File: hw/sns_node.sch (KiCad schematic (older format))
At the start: 1 part

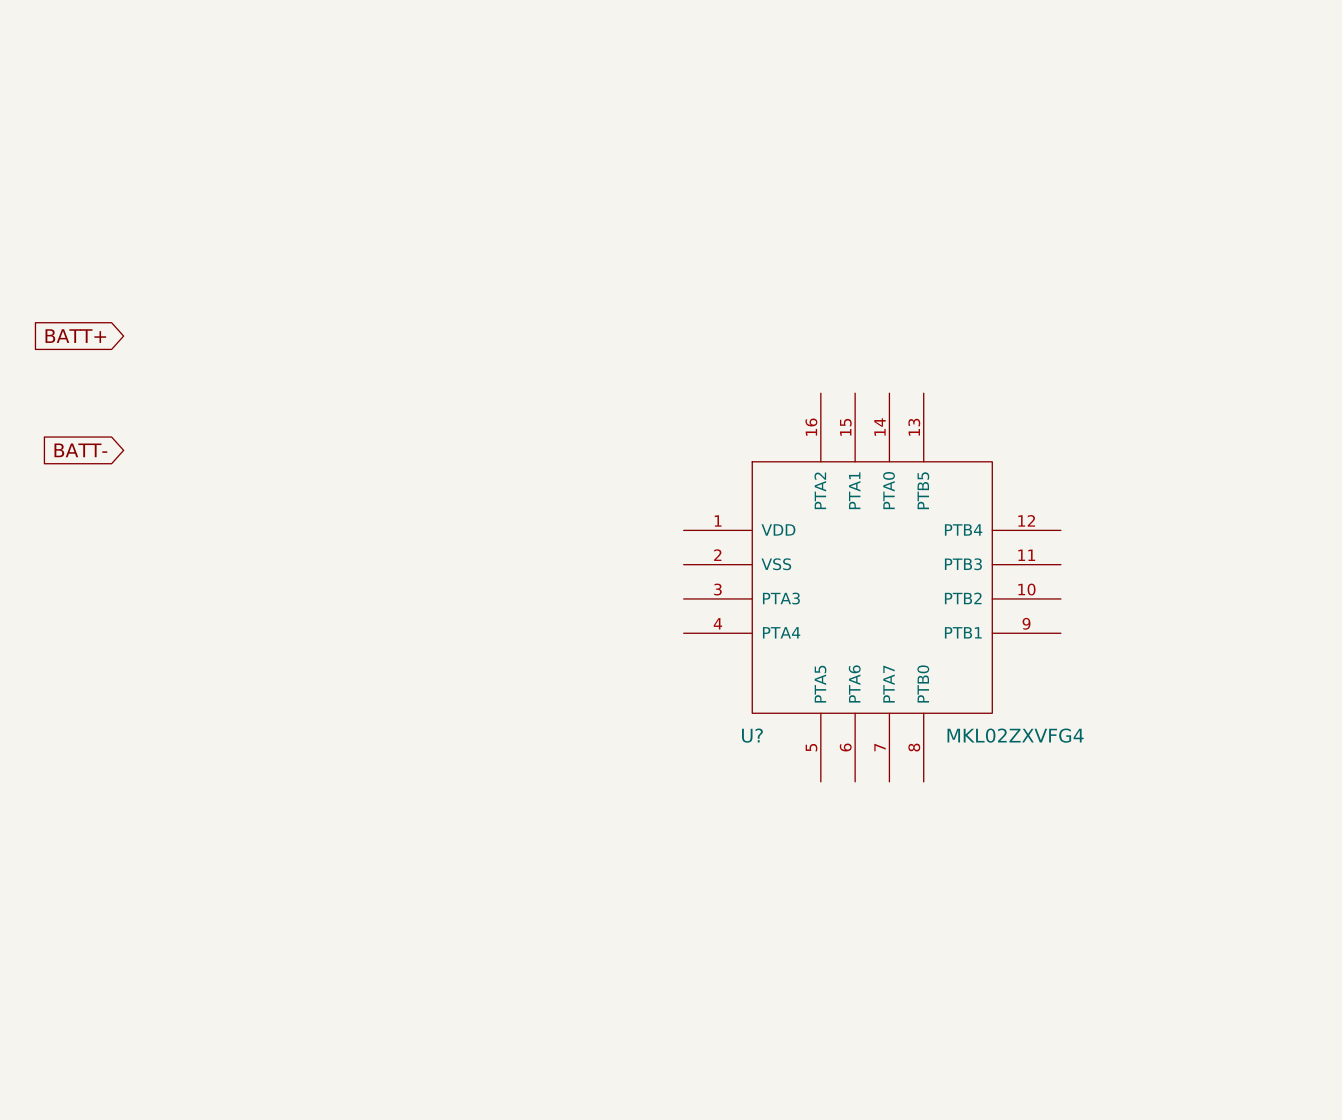
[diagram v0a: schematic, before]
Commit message: - add power supply
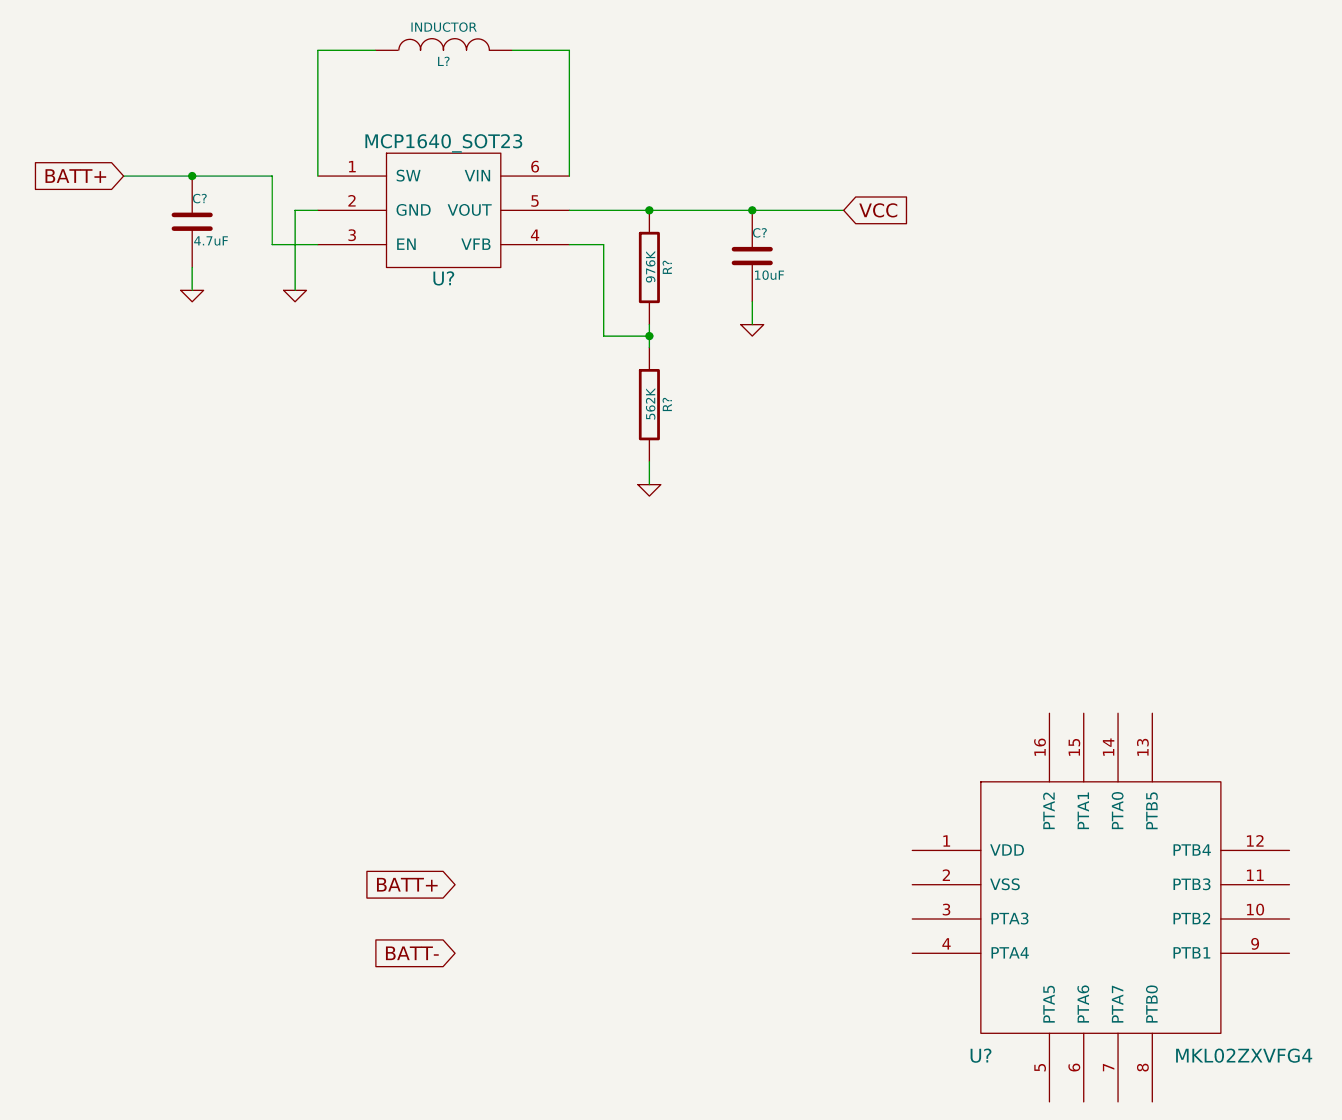
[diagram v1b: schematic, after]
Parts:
- added C?: 4.7uF, ~, symbol C
- added C?: 10uF, ~, symbol C
- added L?: INDUCTOR, ~, symbol INDUCTOR
- added R?: 976K, ~, symbol R
- added R?: 562K, ~, symbol R
- added U?: MCP1640_SOT23, ~, symbol MCP1640_SOT23
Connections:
- net BATT+: now also C?.1, U?.3 (EN)
- new net: L?.1, U?.1 (SW)
- new net: R?.1, R?.2, U?.4 (VFB)
- new net: L?.2, U?.6 (VIN)
- new net GND: C?.2, C?.2, R?.2, U?.2 (GND)
- new net VCC: C?.1, R?.1, U?.5 (VOUT)
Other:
- moved on the sheet: U?
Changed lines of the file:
@@
 L MKL02ZXVFG4 U?
 U 1 1 5302BE68
-P 5400 3350
-F 0 "U?" H 4950 2750 60  0000 C CNN
-F 1 "MKL02ZXVFG4" H 6100 2750 60  0000 C CNN
-F 2 "" H 5400 3350 60  0000 C CNN
-F 3 "" H 5400 3350 60  0000 C CNN
-	1    5400 3350
+P 6400 4750
+F 0 "U?" H 5950 4150 60  0000 C CNN
+F 1 "MKL02ZXVFG4" H 7100 4150 60  0000 C CNN
+F 2 "" H 6400 4750 60  0000 C CNN
+F 3 "" H 6400 4750 60  0000 C CNN
+	1    6400 4750
 	1    0    0    -1
 $EndComp
-Text GLabel 2200 2200 0    60   Input ~ 0
+Text GLabel 2200 1500 0    60   Input ~ 0
 BATT+
-Text GLabel 2200 2700 0    60   Input ~ 0
+Text GLabel 3650 4900 0    60   Input ~ 0
 BATT-
+$Comp
+L MCP1640_SOT23 U?
+U 1 1 5302BFBE
+P 3600 1650
+F 0 "U?" H 3600 1350 60  0000 C CNN
+F 1 "MCP1640_SOT23" H 3600 1950 60  0000 C CNN
+F 2 "~" H 3600 1650 60  0000 C CNN
+F 3 "~" H 3600 1650 60  0000 C CNN
+	1    3600 1650
+	1    0    0    -1
+$EndComp
+$Comp
+L C C?
+U 1 1 5302BFF0
+P 2500 1700
+F 0 "C?" H 2500 1800 40  0000 L CNN
+F 1 "4.7uF" H 2506 1615 40  0000 L CNN
+F 2 "~" H 2538 1550 30  0000 C CNN
+F 3 "~" H 2500 1700 60  0000 C CNN
+	1    2500 1700
+	1    0    0    -1
+$EndComp
+$Comp
+L GND #PWR?
+U 1 1 5302BFFF
+P 2950 2000
+F 0 "#PWR?" H 2950 2000 30  0001 C CNN
+F 1 "GND" H 2950 1930 30  0001 C CNN
+F 2 "" H 2950 2000 60  0000 C CNN
+F 3 "" H 2950 2000 60  0000 C CNN
+	1    2950 2000
+	1    0    0    -1
+$EndComp
+Wire Wire Line
+	3050 1650 2950 1650
+Wire Wire Line
+	2950 1650 2950 2000
+Wire Wire Line
+	3050 1800 2850 1800
+$Comp
+L INDUCTOR L?
+U 1 1 5302C05C
+P 3600 950
+F 0 "L?" V 3550 950 40  0000 C CNN
+F 1 "INDUCTOR" V 3700 950 40  0000 C CNN
+F 2 "~" H 3600 950 60  0000 C CNN
+F 3 "~" H 3600 950 60  0000 C CNN
+	1    3600 950
+	0    -1   -1   0
+$EndComp
+Text GLabel 3650 4600 0    60   Input ~ 0
+BATT+
+Wire Wire Line
+	2200 1500 2850 1500
+$Comp
+L GND #PWR?
+U 1 1 5302C089
+P 2500 2000
+F 0 "#PWR?" H 2500 2000 30  0001 C CNN
+F 1 "GND" H 2500 1930 30  0001 C CNN
+F 2 "" H 2500 2000 60  0000 C CNN
+F 3 "" H 2500 2000 60  0000 C CNN
+	1    2500 2000
+	1    0    0    -1
+$EndComp
+Wire Wire Line
+	2500 1900 2500 2000
+Wire Wire Line
+	2850 1500 2850 1800
+Connection ~ 2500 1500
+Wire Wire Line
+	3300 950  3050 950
+Wire Wire Line
+	3050 950  3050 1500
+Wire Wire Line
+	3900 950  4150 950
+Wire Wire Line
+	4150 950  4150 1500
+$Comp
+L R R?
+U 1 1 5302C0C2
+P 4500 1900
+F 0 "R?" V 4580 1900 40  0000 C CNN
+F 1 "976K" V 4507 1901 40  0000 C CNN
+F 2 "~" V 4430 1900 30  0000 C CNN
+F 3 "~" H 4500 1900 30  0000 C CNN
+	1    4500 1900
+	1    0    0    -1
+$EndComp
+$Comp
+L R R?
+U 1 1 5302C0D6
+P 4500 2500
+F 0 "R?" V 4580 2500 40  0000 C CNN
+F 1 "562K" V 4507 2501 40  0000 C CNN
+F 2 "~" V 4430 2500 30  0000 C CNN
+F 3 "~" H 4500 2500 30  0000 C CNN
+	1    4500 2500
+	1    0    0    -1
+$EndComp
+$Comp
+L GND #PWR?
+U 1 1 5302C0E1
+P 4500 2850
+F 0 "#PWR?" H 4500 2850 30  0001 C CNN
+F 1 "GND" H 4500 2780 30  0001 C CNN
+F 2 "" H 4500 2850 60  0000 C CNN
+F 3 "" H 4500 2850 60  0000 C CNN
+	1    4500 2850
+	1    0    0    -1
+$EndComp
+Wire Wire Line
+	4500 2850 4500 2750
+Wire Wire Line
+	4500 2250 4500 2150
+Wire Wire Line
+	4150 1800 4300 1800
+Wire Wire Line
+	4300 1800 4300 2200
+Wire Wire Line
+	4300 2200 4500 2200
+Connection ~ 4500 2200
+Wire Wire Line
+	4150 1650 5350 1650
+$Comp
+L C C?
+U 1 1 5302C132
+P 4950 1850
+F 0 "C?" H 4950 1950 40  0000 L CNN
+F 1 "10uF" H 4956 1765 40  0000 L CNN
+F 2 "~" H 4988 1700 30  0000 C CNN
+F 3 "~" H 4950 1850 60  0000 C CNN
+	1    4950 1850
+	1    0    0    -1
+$EndComp
+$Comp
+L GND #PWR?
+U 1 1 5302C147
+P 4950 2150
+F 0 "#PWR?" H 4950 2150 30  0001 C CNN
+F 1 "GND" H 4950 2080 30  0001 C CNN
+F 2 "" H 4950 2150 60  0000 C CNN
+F 3 "" H 4950 2150 60  0000 C CNN
+	1    4950 2150
+	1    0    0    -1
+$EndComp
+Wire Wire Line
+	4950 2150 4950 2050
+Connection ~ 4500 1650
+Text GLabel 5350 1650 2    60   Input ~ 0
+VCC
+Connection ~ 4950 1650
 $EndSCHEMATC

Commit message: - add pfet to control en signal
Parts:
- added P?: BATT+, ~, symbol TST
- added P?: BATT-, ~, symbol TST
- added Q?: MOSFET_P, ~, symbol MOSFET_P
- added R?: 1M, ~, symbol R
- gave numbers to parts that had none: 1
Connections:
- net BATT+: now also 4.7uH.2, U?.6 (VIN), P?.1, R?.1; no longer U?.3 (EN)
- net BATT-: now also P?.1
- net GND: now also U?.2 (VSS), Q?.S
- net VCC: now also U?.1 (VDD)
- new net EN: Q?.D, R?.2, U?.3 (EN)
- new net EN_CTRL: Q?.G
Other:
- moved on the sheet: 4.7uH, C?, R?, U?

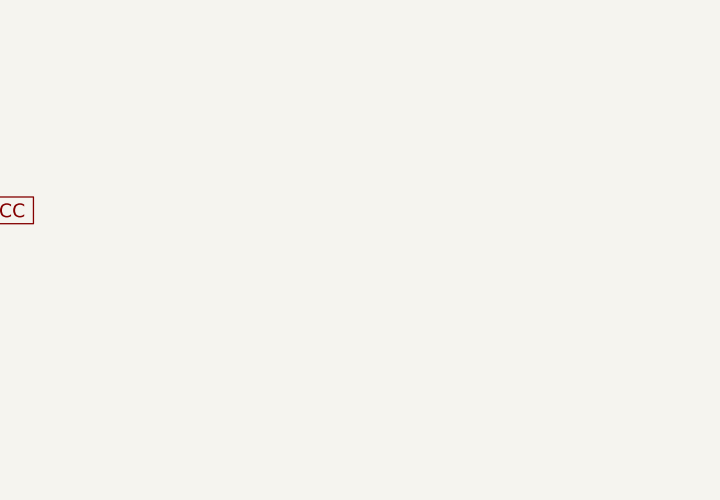
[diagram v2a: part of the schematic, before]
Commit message: - add header for 24l01
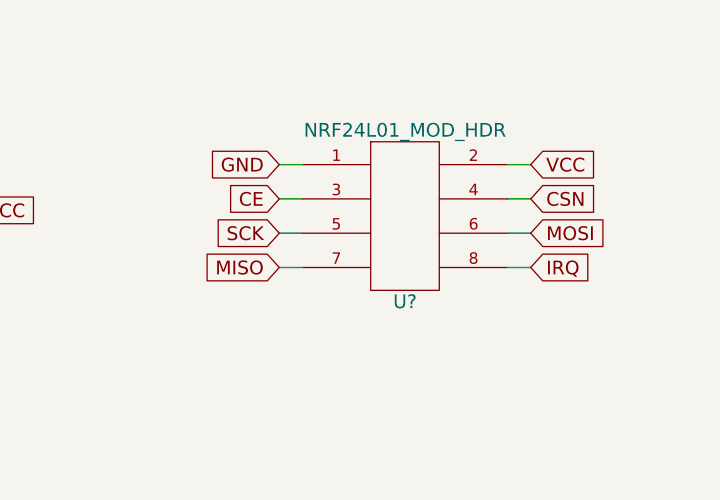
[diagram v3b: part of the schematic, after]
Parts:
- added U?: NRF24L01_MOD_HDR, ~, symbol 2X4_HDR
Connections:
- net GND: now also U?.1
- net VCC: now also U?.2
- new net CE: U?.3
- new net CSN: U?.4
- new net IRQ: U?.8
- new net MISO: U?.7
- new net MOSI: U?.6
- new net SCK: U?.5
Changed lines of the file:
@@
 LIBS:valves
 LIBS:kicadlib
+LIBS:sns_node-cache
 EELAYER 27 0
 EELAYER END
@@
 Sheet 1 1
 Title ""
-Date "18 feb 2014"
+Date "20 feb 2014"
 Rev ""
 Comp ""
@@
 Wire Wire Line
 	3250 5450 3250 5350
+$Comp
+L 2X4_HDR U?
+U 1 1 53055294
+P 6150 2350
+F 0 "U?" H 6150 2000 60  0000 C CNN
+F 1 "NRF24L01_MOD_HDR" H 6150 2750 60  0000 C CNN
+F 2 "~" H 6050 2100 60  0000 C CNN
+F 3 "~" H 6050 2100 60  0000 C CNN
+	1    6150 2350
+	1    0    0    -1
+$EndComp
+Text GLabel 5600 2100 0    60   Input ~ 0
+GND
+Text GLabel 5600 2250 0    60   Input ~ 0
+CE
+Text GLabel 5600 2400 0    60   Input ~ 0
+SCK
+Text GLabel 5600 2550 0    60   Input ~ 0
+MISO
+Text GLabel 6700 2100 2    60   Input ~ 0
+VCC
+Text GLabel 6700 2250 2    60   Input ~ 0
+CSN
+Text GLabel 6700 2400 2    60   Input ~ 0
+MOSI
+Text GLabel 6700 2550 2    60   Input ~ 0
+IRQ
+Wire Wire Line
+	5600 2100 5700 2100
+Wire Wire Line
+	5700 2250 5600 2250
+Wire Wire Line
+	5600 2400 5700 2400
+Wire Wire Line
+	5700 2550 5600 2550
+Wire Wire Line
+	6600 2100 6700 2100
+Wire Wire Line
+	6700 2250 6600 2250
+Wire Wire Line
+	6600 2400 6700 2400
+Wire Wire Line
+	6700 2550 6600 2550
 $EndSCHEMATC
